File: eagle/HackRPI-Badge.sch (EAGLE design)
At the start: 41 parts, among them J1 FTDI_BASICPTH, J2 SOLDERJUMPERPTH, U2 3.3V, U4 74595, U5 74595, U6 74595, U7 74165DT

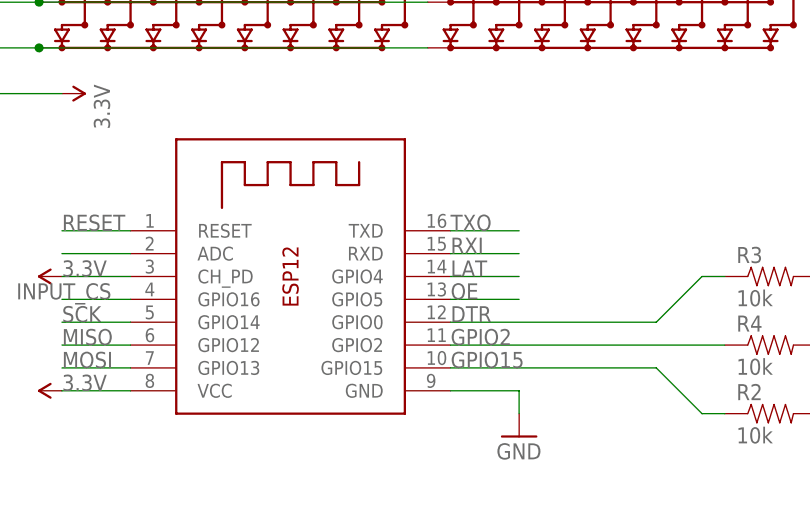
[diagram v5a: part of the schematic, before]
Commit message: Moved ESP module to center-bottom of badge and made the badge smaller, re-routed traces after resizing badge
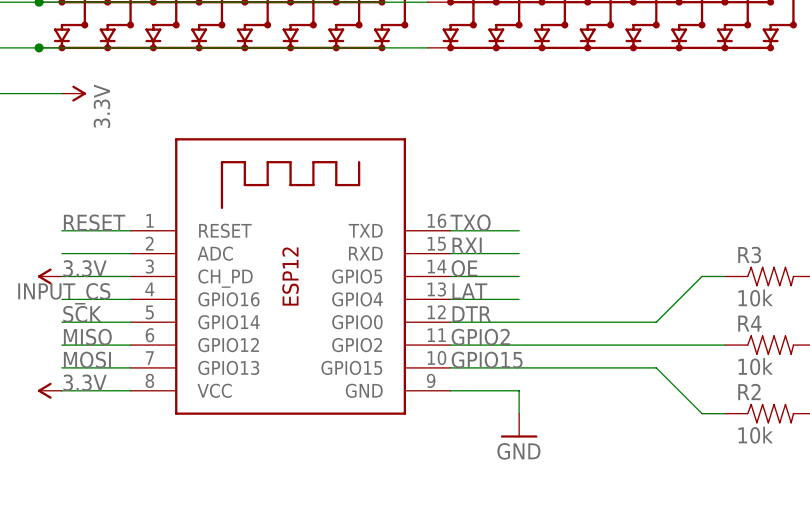
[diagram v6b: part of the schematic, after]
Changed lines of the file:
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@@
-</segment>
-<segment>
-<pinref part="U1" gate="G$1" pin="GPIO4"/>
-<wire x1="17.78" y1="0" x2="25.4" y2="0" width="0.1524" layer="91"/>
-<label x="17.78" y="0" size="1.778" layer="95"/>
 </segment>
 <segment>
@@
 <wire x1="104.14" y1="91.44" x2="91.44" y2="91.44" width="0.1524" layer="91"/>
 <label x="91.44" y="91.44" size="1.778" layer="95"/>
+</segment>
+<segment>
+<pinref part="U1" gate="G$1" pin="GPIO4"/>
+<wire x1="17.78" y1="-2.54" x2="25.4" y2="-2.54" width="0.1524" layer="91"/>
+<label x="17.78" y="-2.54" size="1.778" layer="95"/>
 </segment>
 </net>
@@
 <segment>
 <pinref part="U1" gate="G$1" pin="GPIO5"/>
-<wire x1="17.78" y1="-2.54" x2="25.4" y2="-2.54" width="0.1524" layer="91"/>
-<label x="17.78" y="-2.54" size="1.778" layer="95"/>
+<wire x1="17.78" y1="0" x2="25.4" y2="0" width="0.1524" layer="91"/>
+<label x="17.78" y="0" size="1.778" layer="95"/>
 </segment>
 </net>

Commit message: Fixed LED matrix name typo, updated BOM info for a capacitor
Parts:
- renumbered LEF_RIGHT to LED_RIGHT
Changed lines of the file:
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@@
 <attribute name="PARTNO" value="LDM-13488MI"/>
 </part>
-<part name="LEF_RIGHT" library="mylib" deviceset="8X8LEDMATRIX_COLUMN_CATHODE" device="LDM-13488MI">
+<part name="LED_RIGHT" library="mylib" deviceset="8X8LEDMATRIX_COLUMN_CATHODE" device="LDM-13488MI">
 <attribute name="PARTNO" value="LDM-13488MI"/>
 </part>
@@
 <attribute name="PARTNO" x="-7.62" y="45.72" size="1.778" layer="96" display="off"/>
 </instance>
-<instance part="LEF_RIGHT" gate="G$1" x="35.56" y="45.72">
+<instance part="LED_RIGHT" gate="G$1" x="35.56" y="45.72">
 <attribute name="PARTNO" x="35.56" y="45.72" size="1.778" layer="96" display="off"/>
 </instance>
@@
 <segment>
 <pinref part="LED_LEFT" gate="G$1" pin="R1"/>
-<pinref part="LEF_RIGHT" gate="G$1" pin="R1"/>
+<pinref part="LED_RIGHT" gate="G$1" pin="R1"/>
 <wire x1="-27.94" y1="60.96" x2="15.24" y2="60.96" width="0.1524" layer="91"/>
 <pinref part="U3" gate="G$1" pin="18"/>
@@
 <net name="N$14" class="0">
 <segment>
-<pinref part="LEF_RIGHT" gate="G$1" pin="R2"/>
+<pinref part="LED_RIGHT" gate="G$1" pin="R2"/>
 <pinref part="LED_LEFT" gate="G$1" pin="R2"/>
 <wire x1="15.24" y1="55.88" x2="-27.94" y2="55.88" width="0.1524" layer="91"/>
@@
 <segment>
 <pinref part="LED_LEFT" gate="G$1" pin="R3"/>
-<pinref part="LEF_RIGHT" gate="G$1" pin="R3"/>
+<pinref part="LED_RIGHT" gate="G$1" pin="R3"/>
 <wire x1="-27.94" y1="50.8" x2="15.24" y2="50.8" width="0.1524" layer="91"/>
 <pinref part="U3" gate="G$1" pin="16"/>
@@
 <net name="N$16" class="0">
 <segment>
-<pinref part="LEF_RIGHT" gate="G$1" pin="R4"/>
+<pinref part="LED_RIGHT" gate="G$1" pin="R4"/>
 <pinref part="LED_LEFT" gate="G$1" pin="R4"/>
 <wire x1="15.24" y1="45.72" x2="-27.94" y2="45.72" width="0.1524" layer="91"/>
@@
 <segment>
 <pinref part="LED_LEFT" gate="G$1" pin="R5"/>
-<pinref part="LEF_RIGHT" gate="G$1" pin="R5"/>
+<pinref part="LED_RIGHT" gate="G$1" pin="R5"/>
 <wire x1="-27.94" y1="40.64" x2="15.24" y2="40.64" width="0.1524" layer="91"/>
 <pinref part="U3" gate="G$1" pin="14"/>
@@
 <net name="N$18" class="0">
 <segment>
-<pinref part="LEF_RIGHT" gate="G$1" pin="R6"/>
+<pinref part="LED_RIGHT" gate="G$1" pin="R6"/>
 <pinref part="LED_LEFT" gate="G$1" pin="R6"/>
 <wire x1="15.24" y1="35.56" x2="-27.94" y2="35.56" width="0.1524" layer="91"/>
@@
 <segment>
 <pinref part="LED_LEFT" gate="G$1" pin="R7"/>
-<pinref part="LEF_RIGHT" gate="G$1" pin="R7"/>
+<pinref part="LED_RIGHT" gate="G$1" pin="R7"/>
 <wire x1="-27.94" y1="30.48" x2="15.24" y2="30.48" width="0.1524" layer="91"/>
 <pinref part="U3" gate="G$1" pin="12"/>
@@
 <net name="N$20" class="0">
 <segment>
-<pinref part="LEF_RIGHT" gate="G$1" pin="R8"/>
+<pinref part="LED_RIGHT" gate="G$1" pin="R8"/>
 <pinref part="LED_LEFT" gate="G$1" pin="R8"/>
 <wire x1="15.24" y1="25.4" x2="-27.94" y2="25.4" width="0.1524" layer="91"/>
@@
 <segment>
 <pinref part="RN3" gate="A" pin="1"/>
-<pinref part="LEF_RIGHT" gate="G$1" pin="C1"/>
+<pinref part="LED_RIGHT" gate="G$1" pin="C1"/>
 <wire x1="20.32" y1="68.58" x2="20.32" y2="66.04" width="0.1524" layer="91"/>
 </segment>
@@
 <segment>
 <pinref part="RN3" gate="B" pin="1"/>
-<pinref part="LEF_RIGHT" gate="G$1" pin="C2"/>
+<pinref part="LED_RIGHT" gate="G$1" pin="C2"/>
 <wire x1="25.4" y1="68.58" x2="25.4" y2="66.04" width="0.1524" layer="91"/>
 </segment>
@@
 <segment>
 <pinref part="RN3" gate="C" pin="1"/>
-<pinref part="LEF_RIGHT" gate="G$1" pin="C3"/>
+<pinref part="LED_RIGHT" gate="G$1" pin="C3"/>
 <wire x1="30.48" y1="68.58" x2="30.48" y2="66.04" width="0.1524" layer="91"/>
 </segment>
@@
 <segment>
 <pinref part="RN3" gate="D" pin="1"/>
-<pinref part="LEF_RIGHT" gate="G$1" pin="C4"/>
+<pinref part="LED_RIGHT" gate="G$1" pin="C4"/>
 <wire x1="35.56" y1="68.58" x2="35.56" y2="66.04" width="0.1524" layer="91"/>
 </segment>
@@
 <segment>
 <pinref part="RN4" gate="A" pin="1"/>
-<pinref part="LEF_RIGHT" gate="G$1" pin="C5"/>
+<pinref part="LED_RIGHT" gate="G$1" pin="C5"/>
 <wire x1="40.64" y1="68.58" x2="40.64" y2="66.04" width="0.1524" layer="91"/>
 </segment>
@@
 <segment>
 <pinref part="RN4" gate="B" pin="1"/>
-<pinref part="LEF_RIGHT" gate="G$1" pin="C6"/>
+<pinref part="LED_RIGHT" gate="G$1" pin="C6"/>
 <wire x1="45.72" y1="68.58" x2="45.72" y2="66.04" width="0.1524" layer="91"/>
 </segment>
@@
 <segment>
 <pinref part="RN4" gate="C" pin="1"/>
-<pinref part="LEF_RIGHT" gate="G$1" pin="C7"/>
+<pinref part="LED_RIGHT" gate="G$1" pin="C7"/>
 <wire x1="50.8" y1="68.58" x2="50.8" y2="66.04" width="0.1524" layer="91"/>
 </segment>
@@
 <segment>
 <pinref part="RN4" gate="D" pin="1"/>
-<pinref part="LEF_RIGHT" gate="G$1" pin="C8"/>
+<pinref part="LED_RIGHT" gate="G$1" pin="C8"/>
 <wire x1="55.88" y1="68.58" x2="55.88" y2="66.04" width="0.1524" layer="91"/>
 </segment>
